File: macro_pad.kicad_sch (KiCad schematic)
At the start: 10 parts, among them SW1 SW_Push, SW2 SW_Push, SW3 SW_Push, SW4 SW_Push, SW5 SW_Push, SW6 SW_Push, SW7 SW_Push, SW8 SW_Push, SW9 SW_Push, U1 MOUDLE-SEEEDUINO-XIAO

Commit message: Improved design
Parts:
- removed SW1, SW2, SW3, SW4, SW5, SW6, SW7, SW8, SW9: SW_Push, symbol Switch:SW_Push
- removed U1: MOUDLE-SEEEDUINO-XIAO, XIAO_RP2040:XIAO-Generic-Hybrid-14P-2.54-21X17.8MM, symbol XIAO_RP2040:MOUDLE-SEEEDUINO-XIAO
- added A1: RaspberryPi_Pico, Module:RaspberryPi_Pico_SMD, symbol MCU_Module:RaspberryPi_Pico_Extensive
- added D1, D10, D11, D12, D13, D14, D15, D16, D2, D3, D4, D5, D6, D7, D8, D9: D_Small_Filled, Diode_THT:D_DO-35_SOD27_P7.62mm_Horizontal, symbol Device:D_Small_Filled
- added D17, D18, D19, D20, D21, D22, D23, D24, D25, D26, D27, D28: SK6812MINI-E, SK6812MINI-E:SK6812MINI-E_fixed, symbol SK6812MINI-E:SK6812MINI-E
- added J1: OLED, Connector_PinSocket_2.54mm:PinSocket_1x04_P2.54mm_Vertical, symbol Connector:Conn_01x04_Socket
- added J2: SWD, Connector_PinHeader_2.54mm:PinHeader_1x04_P2.54mm_Vertical, symbol Connector:Conn_01x04_Pin
- added R1: 500, Resistor_THT:R_Axial_DIN0204_L3.6mm_D1.6mm_P7.62mm_Horizontal, symbol Device:R
- added R2, R3: 2k2, Resistor_THT:R_Axial_DIN0204_L3.6mm_D1.6mm_P7.62mm_Horizontal, symbol Device:R
- added SW1, SW10, SW11, SW12, SW13, SW14, SW15, SW16, SW2, SW3, SW4, SW5, SW6, SW7, SW8, SW9: SW_Push_45deg, Button_Switch_Keyboard:SW_Cherry_MX_1.00u_PCB, symbol Switch:SW_Push_45deg
- added SW17, SW18: RotaryEncoder_Switch, RotaryEncoder_Alps_EC11E-Switch_Vertical_H20mm:RotaryEncoder_Alps_EC11E-Switch_Vertical_H20mm, symbol Device:RotaryEncoder_Switch
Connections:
- new net: D14.2 (A), SW14.2
- new net: D1.2 (A), SW1.2
- new net: D5.2 (A), SW5.2
- new net: D11.2 (A), SW11.2
- new net: D16.2 (A), SW16.2
- new net: D15.2 (A), SW15.2
- new net: D18.2 (DOUT), D19.4 (DIN)
- new net: D17.2 (DOUT), D18.4 (DIN)
- new net: D6.2 (A), SW6.2
- new net: D12.2 (A), SW12.2
- new net: D2.2 (A), SW2.2
- new net: D3.2 (A), SW3.2
- new net: D4.2 (A), SW4.2
- new net: D9.2 (A), SW9.2
- new net: D7.2 (A), SW7.2
- new net: D19.2 (DOUT), D20.4 (DIN)
- new net: D8.2 (A), SW8.2
- new net: D27.2 (DOUT), D28.4 (DIN)
- new net: D26.2 (DOUT), D27.4 (DIN)
- new net: D25.2 (DOUT), D26.4 (DIN)
- new net: D21.2 (DOUT), D22.4 (DIN)
- new net: D20.2 (DOUT), D21.4 (DIN)
- new net: D13.2 (A), SW13.2
- new net: D10.2 (A), SW10.2
- new net: D22.2 (DOUT), D23.4 (DIN)
- new net: D24.2 (DOUT), D25.4 (DIN)
- new net: D23.2 (DOUT), D24.4 (DIN)
- new net: D17.4 (DIN), R1.2
- new net +3V3: A1.36 (3V3), J2.4 (Pin_4)
- new net +5V: A1.40 (VBUS), D17.1 (VDD), D18.1 (VDD), D19.1 (VDD), D20.1 (VDD), D21.1 (VDD), D22.1 (VDD), D23.1 (VDD), D24.1 (VDD), D25.1 (VDD), D26.1 (VDD), D27.1 (VDD), D28.1 (VDD), J1.3 (Pin_3), R2.2, R3.2
- new net BrEncA: A1.16 (GPIO12), SW18.A
- new net BrEncB: A1.17 (GPIO13), SW18.B
- new net EncB1: A1.19 (GPIO14), SW17.S1
- new net EncB2: A1.20 (GPIO15), SW18.S1
- new net GND: A1.13 (GND), A1.18 (GND), A1.23 (GND), A1.28 (GND), A1.3 (GND), A1.38 (GND), A1.8 (GND), A1.D2 (GND), D17.3 (VSS), D18.3 (VSS), D19.3 (VSS), D20.3 (VSS), D21.3 (VSS), D22.3 (VSS), D23.3 (VSS), D24.3 (VSS), D25.3 (VSS), D26.3 (VSS), D27.3 (VSS), D28.3 (VSS), J1.4 (Pin_4), J2.1 (Pin_1), SW17.C, SW17.S2, SW18.C, SW18.S2
- new net LedData: A1.21 (GPIO16), R1.1
- new net SCL: A1.2 (GPIO1), J1.2 (Pin_2), R3.1
- new net SDA: A1.1 (GPIO0), J1.1 (Pin_1), R2.1
- new net SWCLK: A1.D1 (SWCLK), J2.3 (Pin_3)
- new net SWDIO: A1.D3 (SWDIO), J2.2 (Pin_2)
- new net VlEncA: A1.14 (GPIO10), SW17.A
- new net VlEncB: A1.15 (GPIO11), SW17.B
- new net column0: A1.4 (GPIO2), SW1.1, SW13.1, SW5.1, SW9.1
- new net column1: A1.5 (GPIO3), SW10.1, SW14.1, SW2.1, SW6.1
- new net column2: A1.6 (GPIO4), SW11.1, SW15.1, SW3.1, SW7.1
- new net column3: A1.7 (GPIO5), SW12.1, SW16.1, SW4.1, SW8.1
- new net row0: A1.9 (GPIO6), D1.1 (K), D2.1 (K), D3.1 (K), D4.1 (K)
- new net row1: A1.10 (GPIO7), D5.1 (K), D6.1 (K), D7.1 (K), D8.1 (K)
- new net row2: A1.11 (GPIO8), D10.1 (K), D11.1 (K), D12.1 (K), D9.1 (K)
- new net row3: A1.12 (GPIO9), D13.1 (K), D14.1 (K), D15.1 (K), D16.1 (K)
- no-connect marks 0 -> 1
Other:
- company: (none) -> Hackclub
- title: (none) -> Macropad

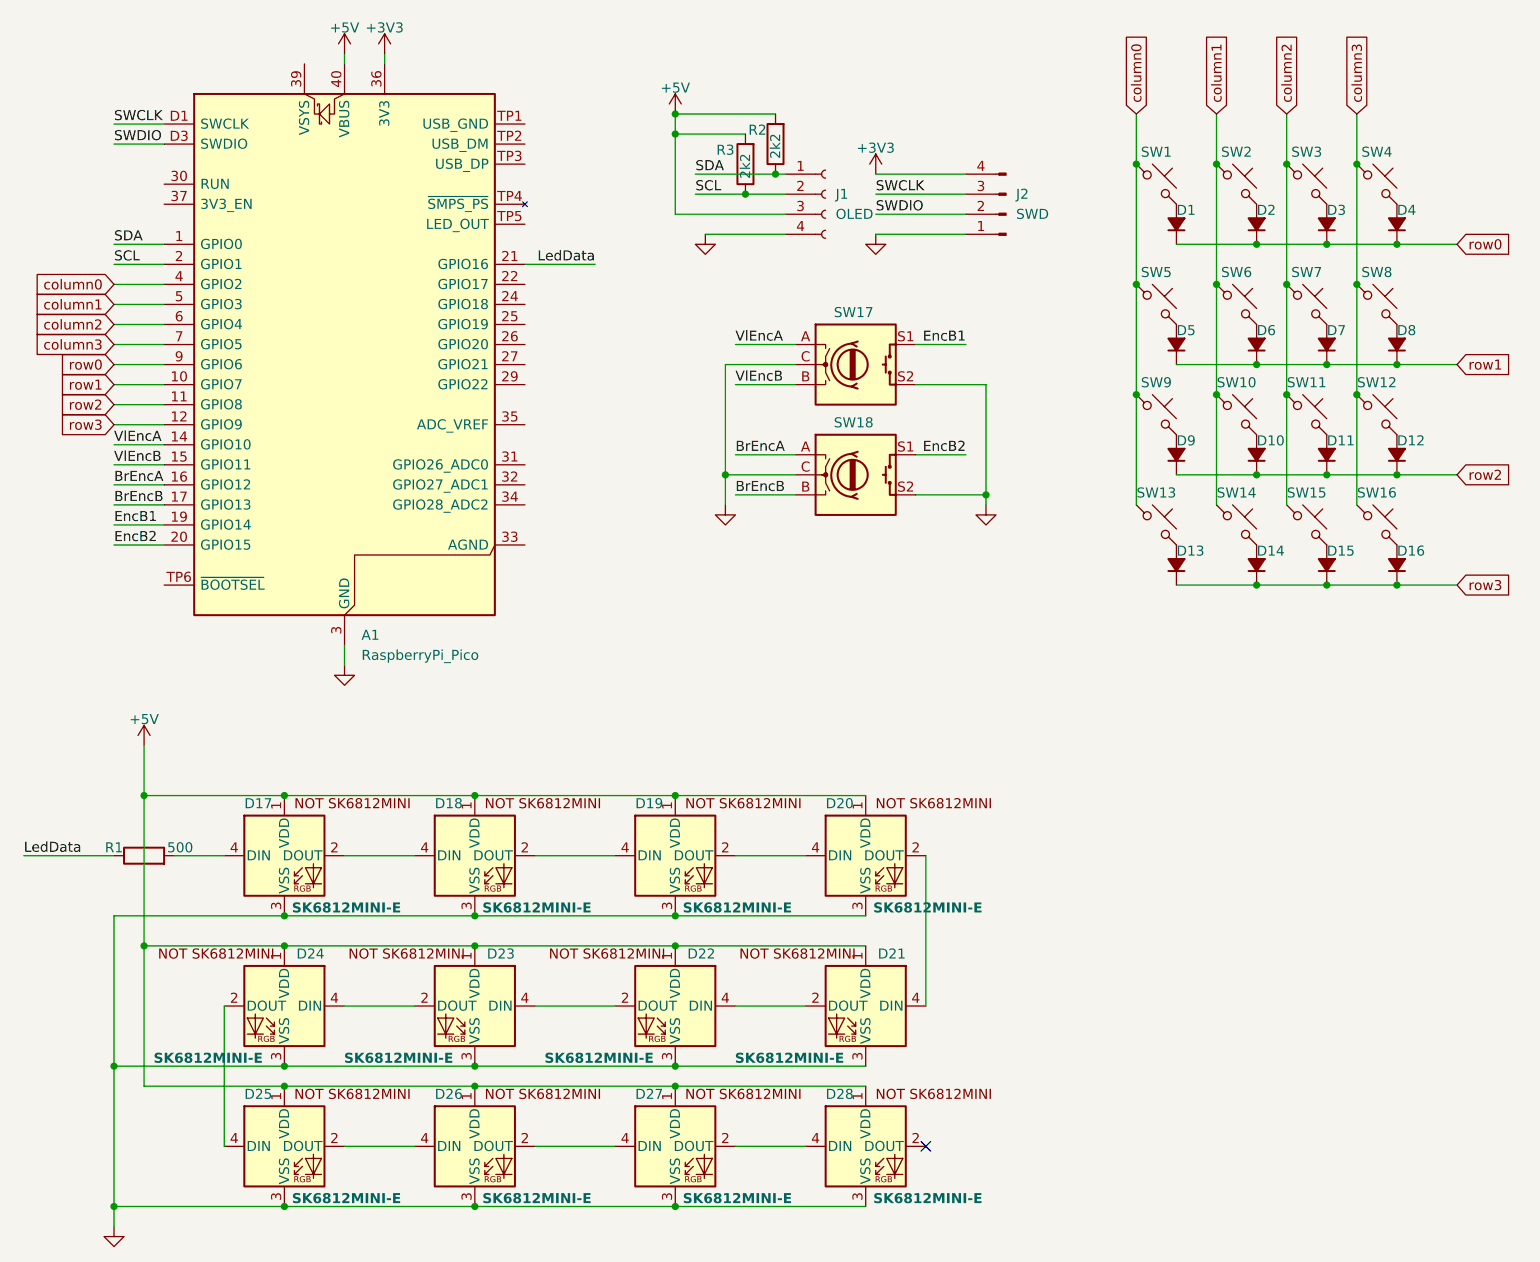
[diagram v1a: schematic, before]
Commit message: Added mounting holes
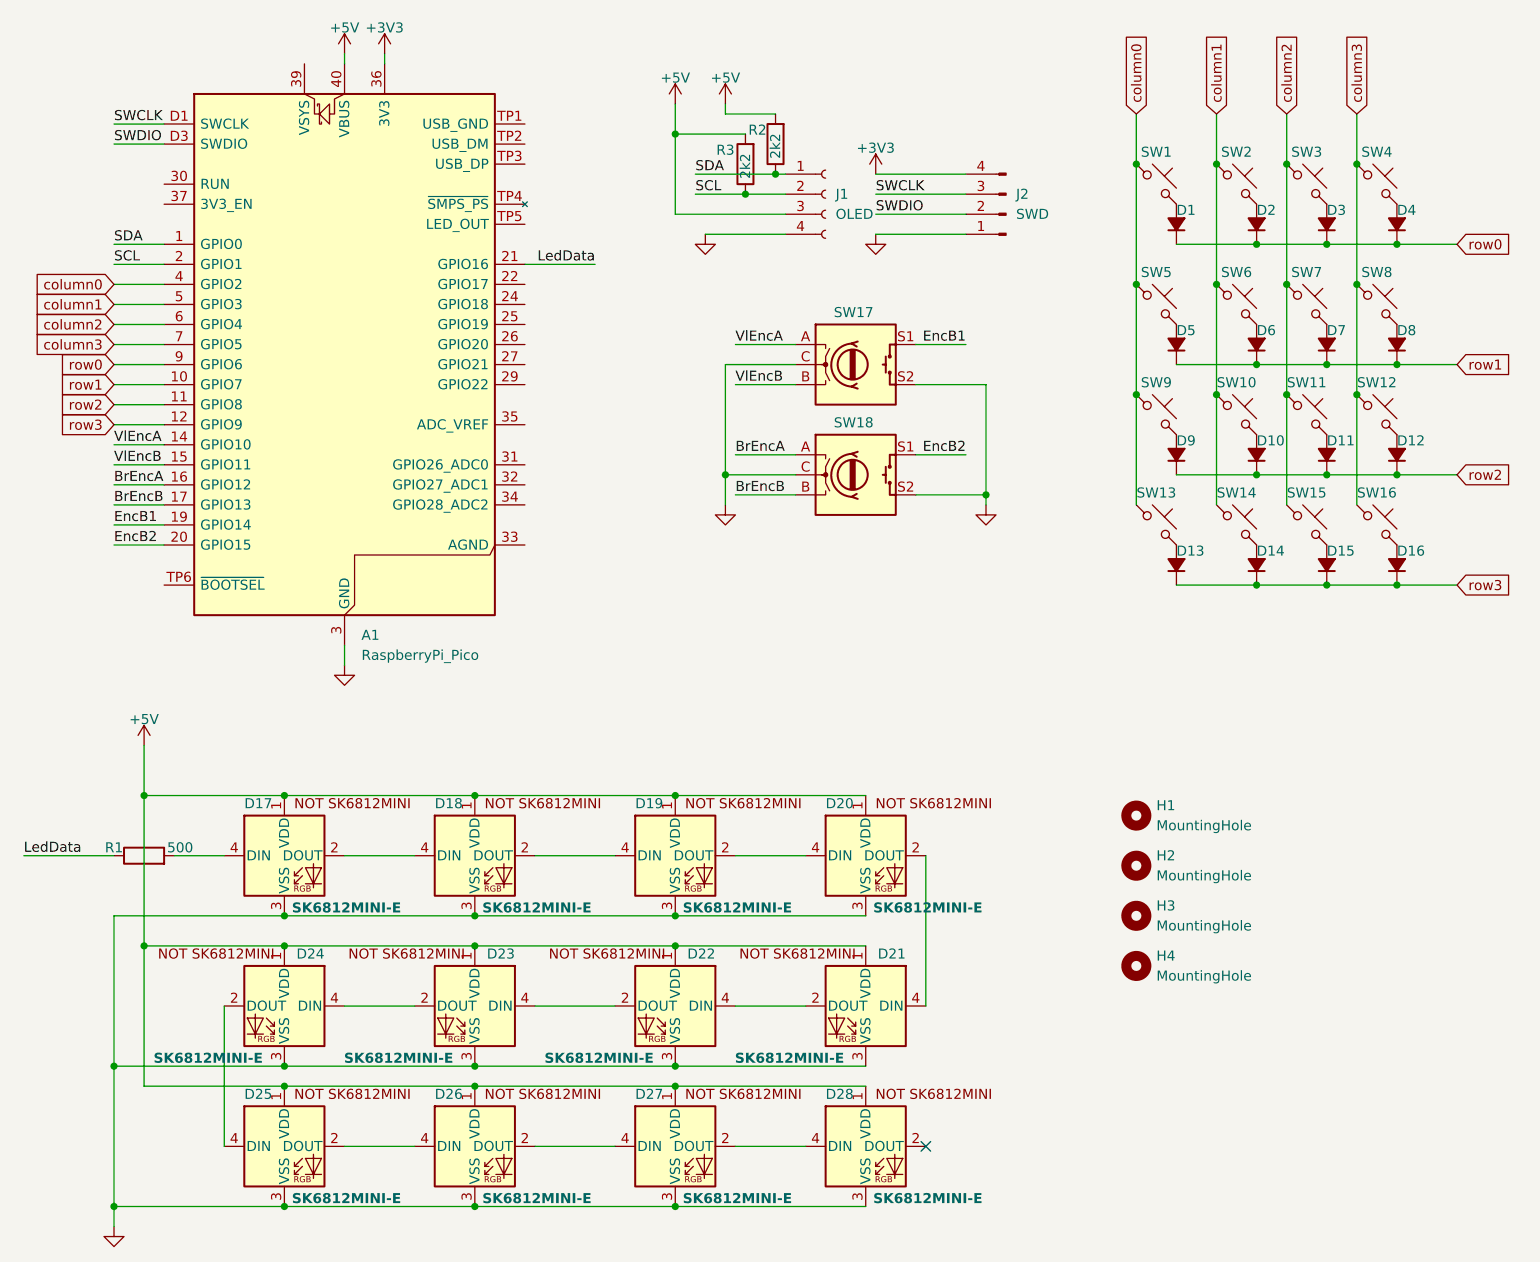
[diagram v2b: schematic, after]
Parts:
- added H1, H2, H3, H4: MountingHole, MountingHole:MountingHole_3.2mm_M3, symbol Mechanical:MountingHole
